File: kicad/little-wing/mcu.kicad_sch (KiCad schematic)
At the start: 29 parts, among them SW2 Reset, U1 ${ALTIUM_VALUE}, X1 ${ALTIUM_VALUE}, X2 ${ALTIUM_VALUE}

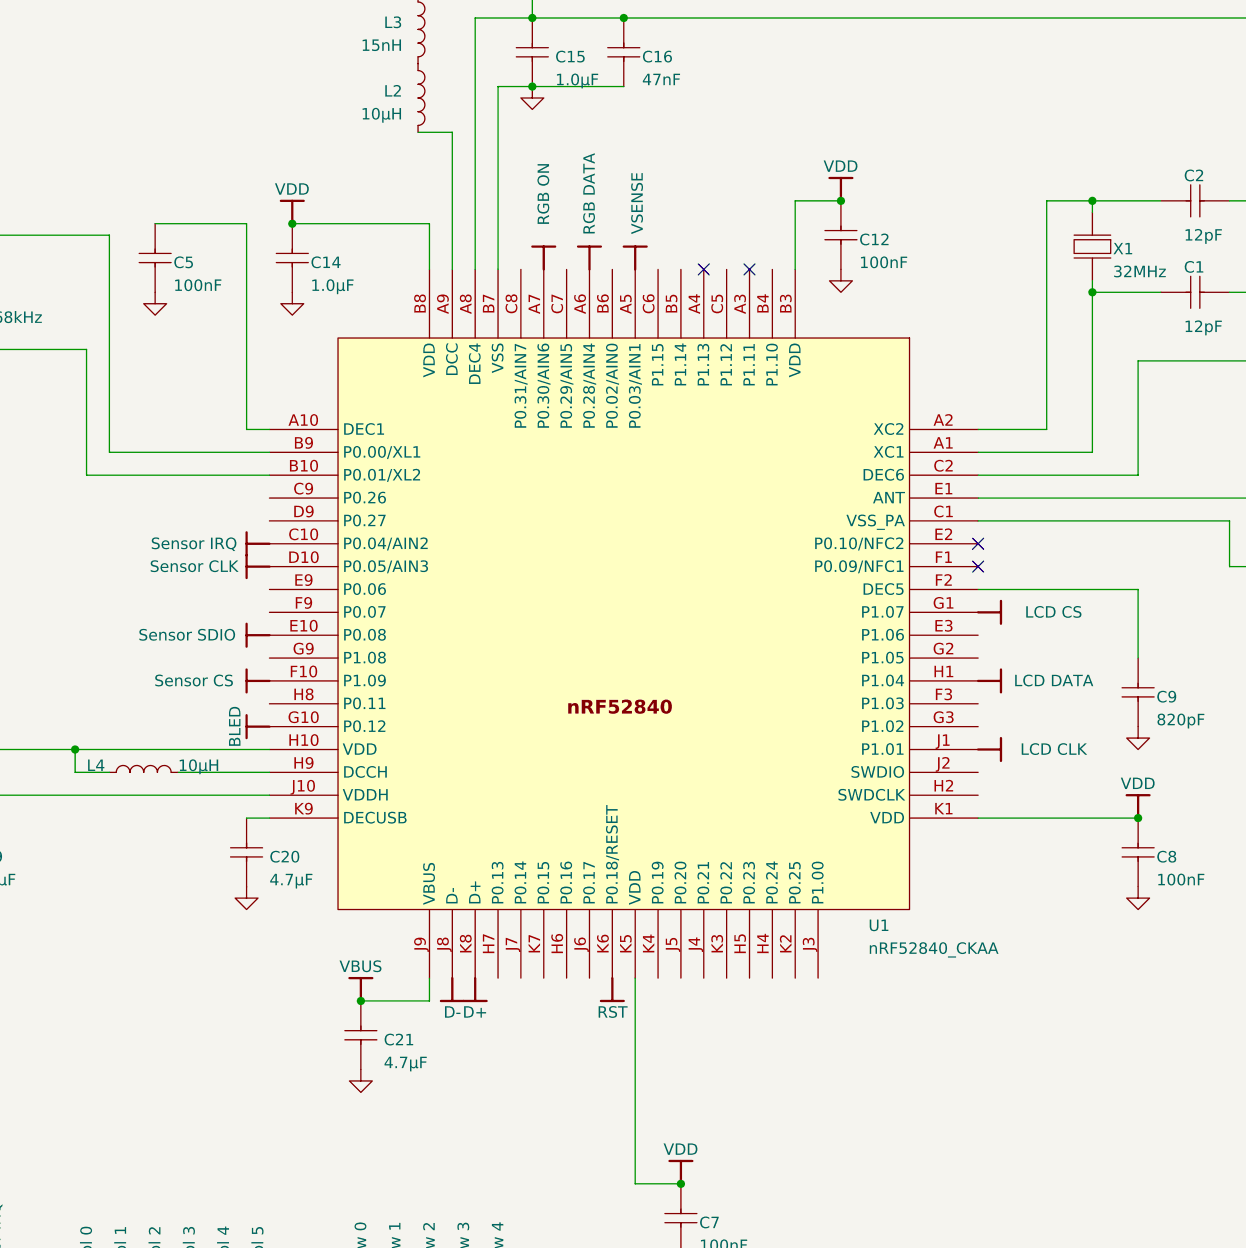
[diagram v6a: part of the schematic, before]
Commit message: Connecting remaining power lines
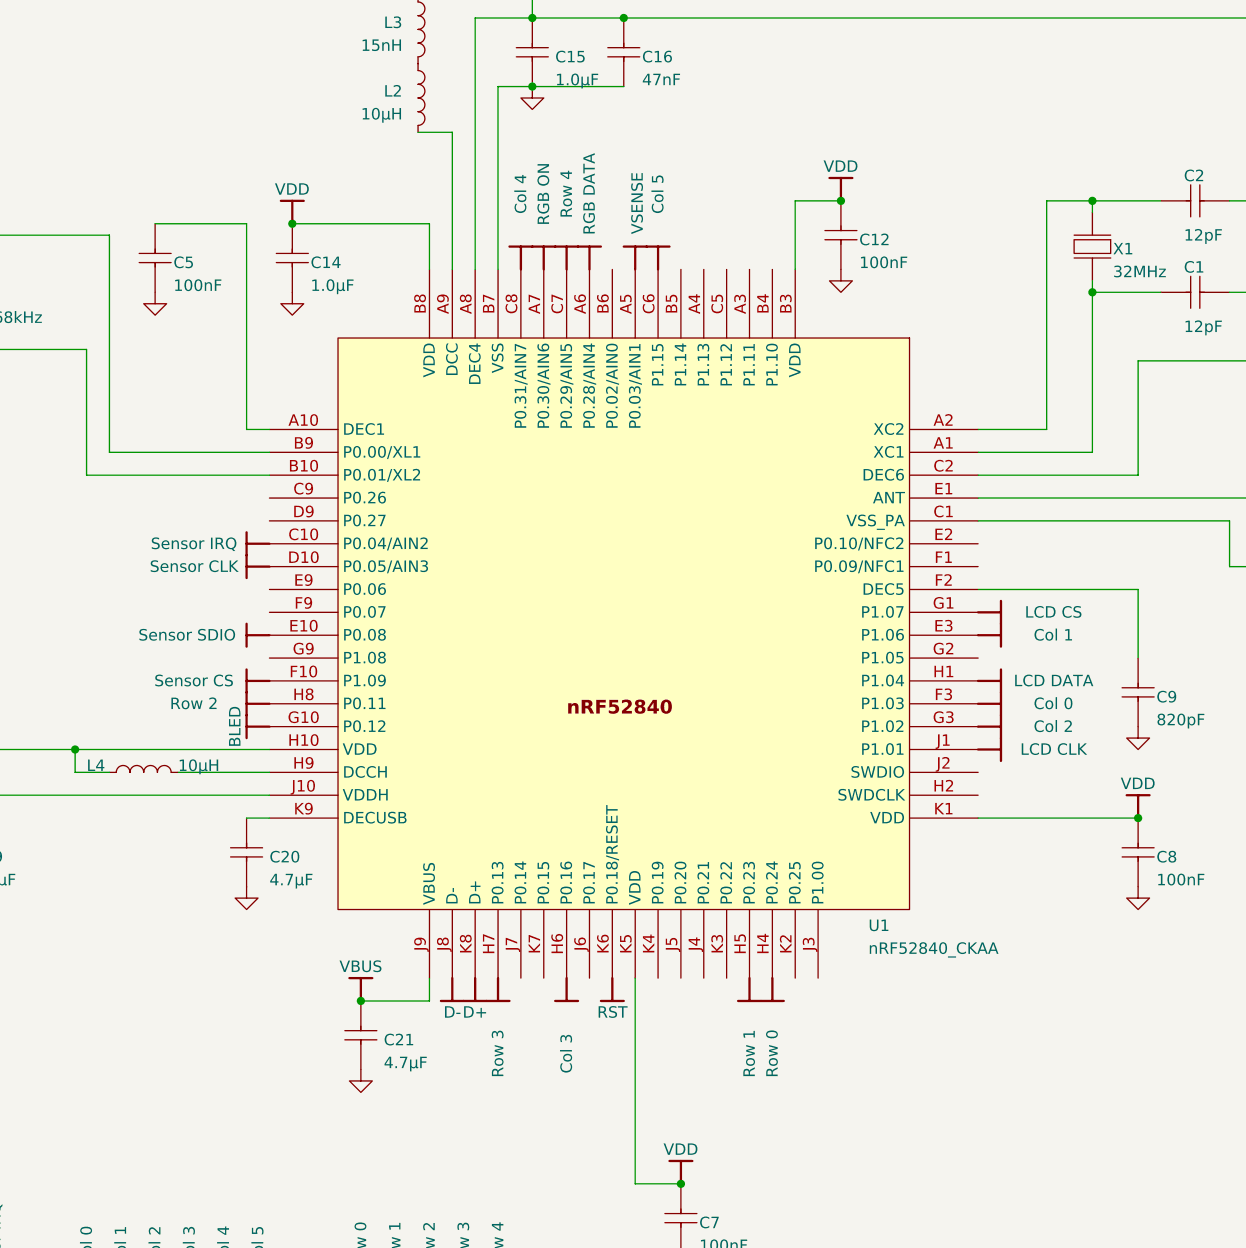
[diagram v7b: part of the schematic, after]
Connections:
- net Col 0: now also U1.F3 (P1.03)
- net Col 1: now also U1.E3 (P1.06)
- net Col 2: now also U1.G3 (P1.02)
- net Col 3: now also U1.H6 (P0.16)
- net Col 4: now also U1.C8 (P0.31/AIN7)
- net Col 5: now also U1.C6 (P1.15)
- net Row 0: now also U1.H4 (P0.24)
- net Row 1: now also U1.H5 (P0.23)
- net Row 2: now also U1.H8 (P0.11)
- net Row 3: now also U1.H7 (P0.13)
- net Row 4: now also U1.C7 (P0.29/AIN5)
- no-connect marks 4 -> 0

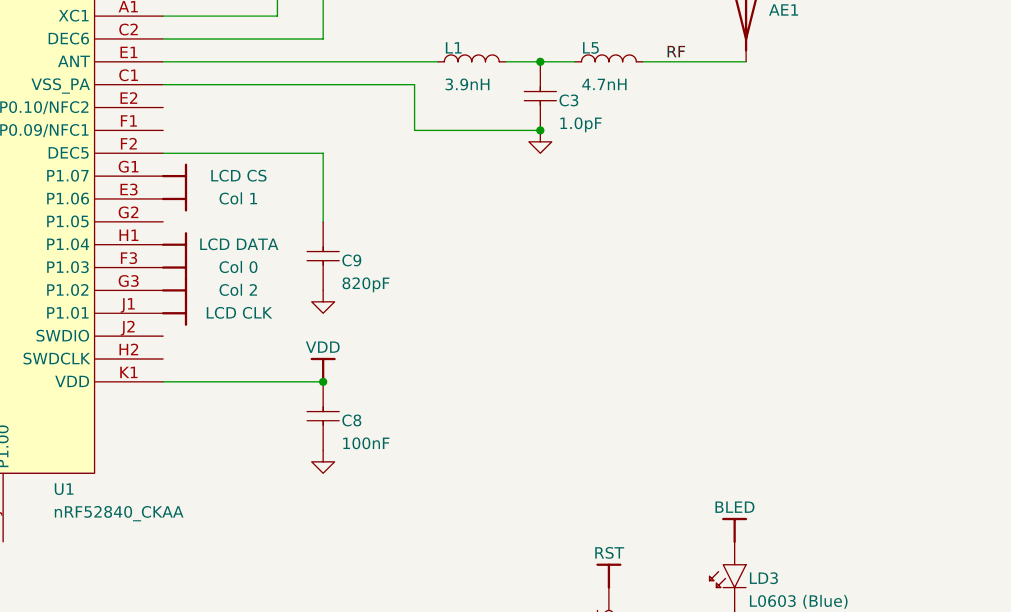
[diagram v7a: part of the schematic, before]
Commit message: Adding the J-tag connector for the programmer
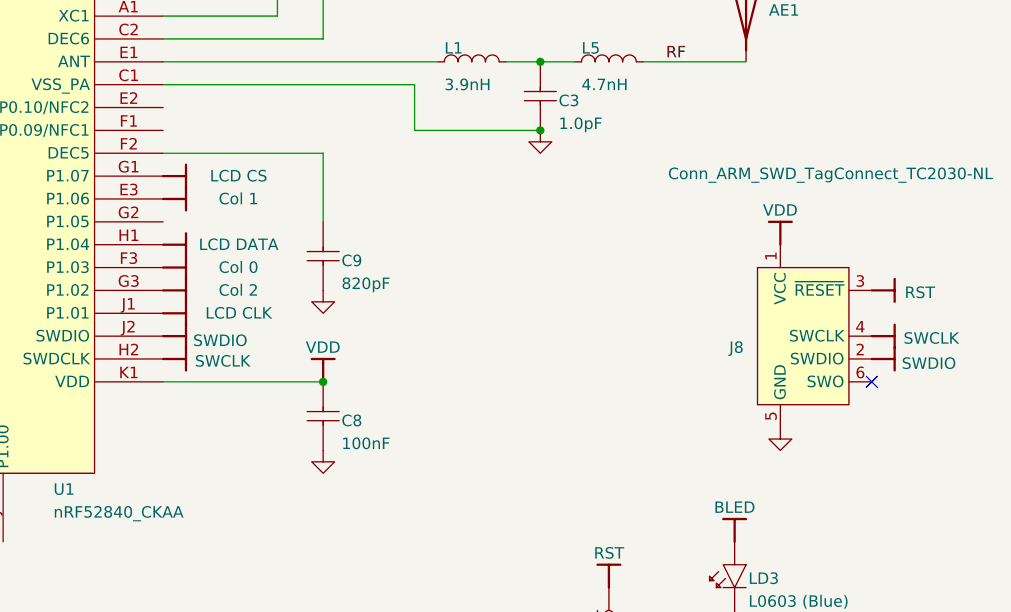
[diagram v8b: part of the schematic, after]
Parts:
- added J8: Conn_ARM_SWD_TagConnect_TC2030-NL, Connector:Tag-Connect_TC2030-IDC-NL_2x03_P1.27mm_Vertical, symbol Connector:Conn_ARM_SWD_TagConnect_TC2030-NL
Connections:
- net GND: now also J8.5 (GND)
- net RST: now also J8.3 (~{RESET})
- net VDD: now also J8.1 (VCC)
- net SWCLK: now reaches U1.H2 (SWDCLK)
- net SWCLK: now also J8.4 (SWCLK)
- net SWDIO: now reaches U1.J2 (SWDIO)
- net SWDIO: now also J8.2 (SWDIO)
- no-connect marks 0 -> 1
